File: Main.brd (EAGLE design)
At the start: 100 x 80 mm, 11 parts, among them U2 LM 1084 IT5,0, U3 LM 1084 IT3,3, X1 12V

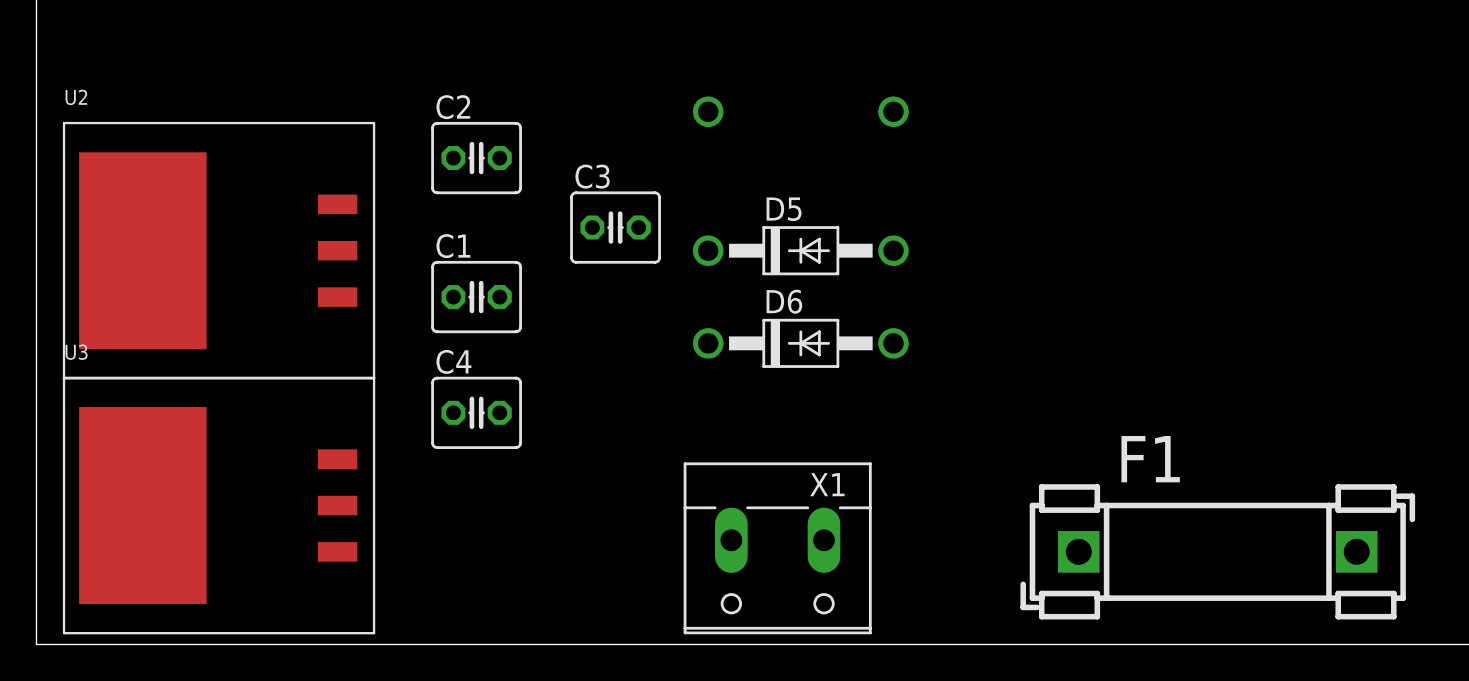
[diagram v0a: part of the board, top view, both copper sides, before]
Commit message: got rid of unneeded junctions
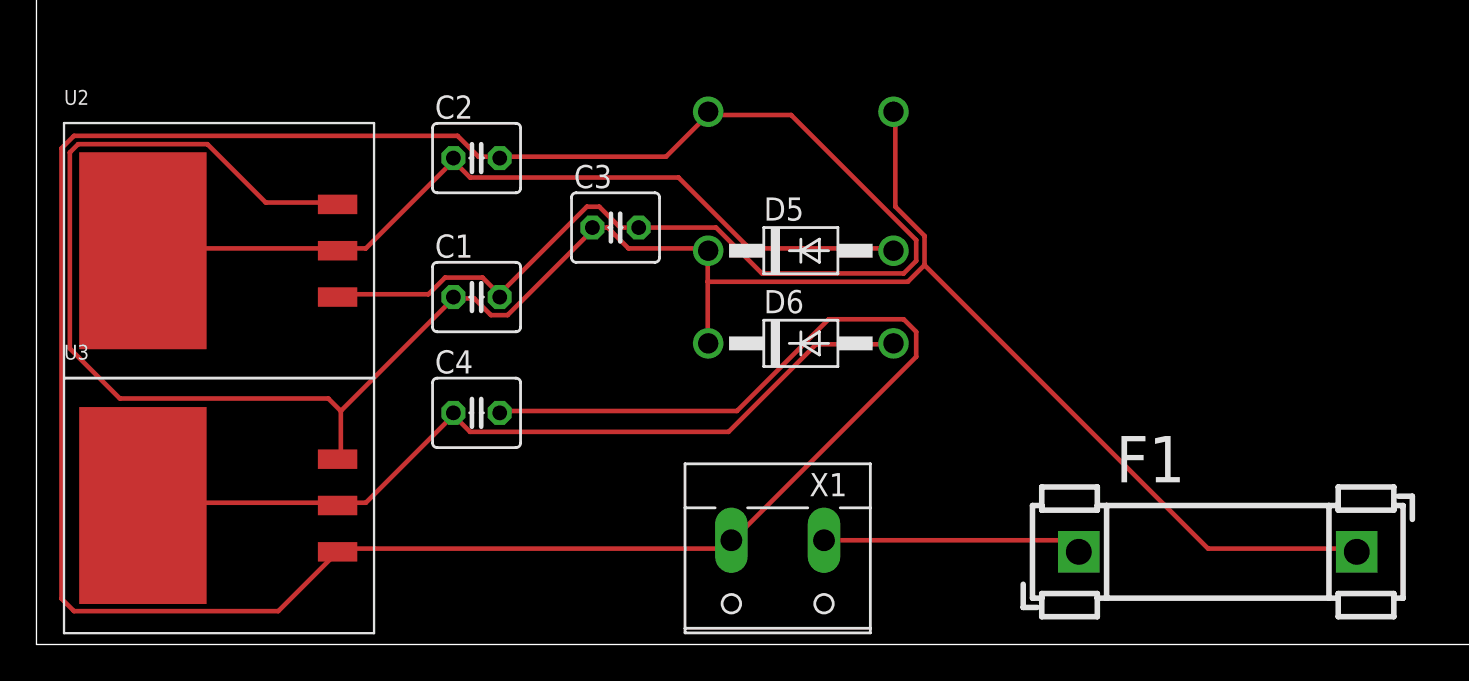
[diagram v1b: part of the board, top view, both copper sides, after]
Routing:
- net N$3: track 0.00 -> 193.5 mm
- net +12V: track 0.00 -> 128.6 mm
- net +3.3V: track 0.00 -> 45.9 mm
- net +5V: track 0.00 -> 45.5 mm
- net N$1: track 0.00 -> 14.3 mm

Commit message: fixed it... misleading warnings due to unneeded wires
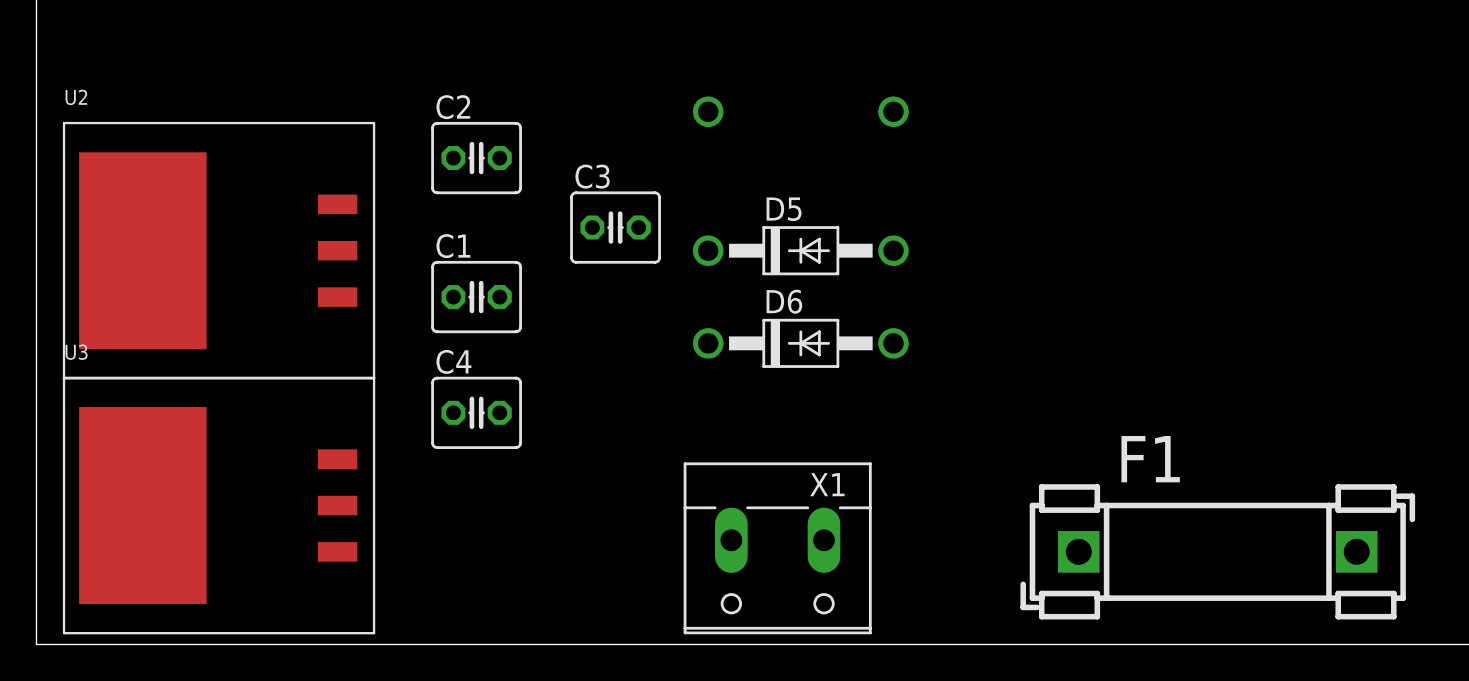
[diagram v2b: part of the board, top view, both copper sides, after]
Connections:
- net N$3 renamed GND
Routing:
- net GND: track 193.5 -> 0.00 mm
- net +12V: track 128.6 -> 0.00 mm
- net +3.3V: track 45.9 -> 0.00 mm
- net +5V: track 45.5 -> 0.00 mm
- net N$1: track 14.3 -> 0.00 mm

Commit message: got rid of hopefully redundant C
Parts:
- removed C3: 10uF Tant., rcl:C025-040X050
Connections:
- net +12V: no longer C3.1
- net GND: no longer C3.2
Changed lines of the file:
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@@
 <element name="C1" library="rcl" package="C025-040X050" value="10uF Tant." x="24.13" y="19.05"/>
 <element name="C2" library="rcl" package="C025-040X050" value="10uF Tant." x="24.13" y="26.67"/>
-<element name="C3" library="rcl" package="C025-040X050" value="10uF Tant." x="31.75" y="22.86"/>
 <element name="C4" library="rcl" package="C025-040X050" value="10uF Tant." x="24.13" y="12.7"/>
 <element name="D5" library="diode" package="DO41-10" value="1N4004" x="41.91" y="21.59"/>
@@
 <contactref element="D6" pad="C"/>
 <contactref element="U3" pad="3"/>
-<contactref element="C1" pad="1"/>
-<contactref element="C3" pad="1"/>
 <contactref element="D5" pad="C"/>
 <contactref element="D1" pad="C"/>
 <contactref element="F1" pad="2"/>
+<contactref element="C1" pad="1"/>
 <wire x1="46.99" y1="29.21" x2="72.39" y2="5.08" width="0" layer="19" extent="1-1"/>
 <wire x1="36.83" y1="21.59" x2="46.99" y2="29.21" width="0" layer="19" extent="1-1"/>
 <wire x1="36.83" y1="16.51" x2="36.83" y2="21.59" width="0" layer="19" extent="1-1"/>
-<wire x1="30.48" y1="22.86" x2="36.83" y2="21.59" width="0" layer="19" extent="1-1"/>
-<wire x1="22.86" y1="19.05" x2="30.48" y2="22.86" width="0" layer="19" extent="1-1"/>
+<wire x1="22.86" y1="19.05" x2="36.83" y2="21.59" width="0" layer="19" extent="1-1"/>
 <wire x1="16.51" y1="24.13" x2="22.86" y2="19.05" width="0" layer="19" extent="1-1"/>
 <wire x1="16.51" y1="10.16" x2="22.86" y2="19.05" width="0" layer="19" extent="1-1"/>
@@
 <signal name="GND">
 <contactref element="X1" pad="2"/>
-<contactref element="C1" pad="2"/>
 <contactref element="C4" pad="2"/>
 <contactref element="C2" pad="2"/>
-<contactref element="C3" pad="2"/>
 <contactref element="U3" pad="1"/>
 <contactref element="U2" pad="1"/>
 <contactref element="D1" pad="A"/>
-<wire x1="33.02" y1="22.86" x2="36.83" y2="29.21" width="0" layer="19" extent="1-1"/>
-<wire x1="25.4" y1="26.67" x2="33.02" y2="22.86" width="0" layer="19" extent="1-1"/>
+<contactref element="C1" pad="2"/>
+<wire x1="25.4" y1="26.67" x2="36.83" y2="29.21" width="0" layer="19" extent="1-1"/>
 <wire x1="25.4" y1="19.05" x2="25.4" y2="26.67" width="0" layer="19" extent="1-1"/>
 <wire x1="25.4" y1="12.7" x2="25.4" y2="19.05" width="0" layer="19" extent="1-1"/>

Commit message: finally got connections without wires
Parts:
- added R1: 4711, resistor:0617/22
- moved F1 90.9 mm to (-31.8, 24.1)
- moved D1 83.9 mm to (-40.6, 44.5), flipped to the top
- moved X1 83.8 mm to (-40.6, 25.4), turned to 0 degrees
- moved D6 82.4 mm to (-31.8, 53.3)
- moved C1 71.8 mm to (-45.7, 35.6)
- moved D5 68.7 mm to (-19.1, 53.3)
- moved C4 63.8 mm to (-30.5, 45.7)
- moved U3 49.5 mm to (-38.1, 7.62)
- moved C2 48.4 mm to (-20.3, 45.7)
- moved U2 34.7 mm to (-20.3, 7.62)
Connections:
- net +12V: now also R1.1
- net GND: now also R1.2
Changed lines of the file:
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@@
 <description language="de">&lt;b&gt;EAGLE Design Rules&lt;/b&gt;
 &lt;p&gt;
-Die Standard-Design-Rules sind so gewÃ¤hlt, dass sie fÃ¼r
+Die Standard-Design-Rules sind so gewählt, dass sie für
 die meisten Anwendungen passen. Sollte ihre Platine
 besondere Anforderungen haben, treffen Sie die erforderlichen
@@
 <autorouter>
 <pass name="Default">
-<param name="RoutingGrid" value="12.5mil"/>
+<param name="RoutingGrid" value="50mil"/>
 <param name="AutoGrid" value="1"/>
 <param name="Efforts" value="0"/>
 <param name="TopRouterVariant" value="1"/>
 <param name="tpViaShape" value="round"/>
-<param name="PrefDir.1" value="|"/>
+<param name="PrefDir.1" value="a"/>
 <param name="PrefDir.2" value="0"/>
 <param name="PrefDir.3" value="0"/>
@@
 <param name="PrefDir.14" value="0"/>
 <param name="PrefDir.15" value="0"/>
-<param name="PrefDir.16" value="0"/>
+<param name="PrefDir.16" value="a"/>
 <param name="cfVia" value="8"/>
 <param name="cfNonPref" value="5"/>
@@
 </autorouter>
 <elements>
-<element name="C1" library="rcl" package="C025-040X050" value="10uF Tant." x="24.13" y="19.05"/>
-<element name="C2" library="rcl" package="C025-040X050" value="10uF Tant." x="24.13" y="26.67"/>
-<element name="C4" library="rcl" package="C025-040X050" value="10uF Tant." x="24.13" y="12.7"/>
-<element name="D5" library="diode" package="DO41-10" value="1N4004" x="41.91" y="21.59"/>
-<element name="D6" library="diode" package="DO41-10" value="1N4004" x="41.91" y="16.51"/>
-<element name="U2" library="PP_PowerIC" package="TO-263-3" value="LM 1084 IT5,0" x="11.43" y="21.59"/>
-<element name="U3" library="PP_PowerIC" package="TO-263-3" value="LM 1084 IT3,3" x="11.43" y="7.62"/>
-<element name="X1" library="con-wago-508" package="W237-132" value="12V" x="40.64" y="5.08" rot="R180">
-<attribute name="OC_NEWARK" value="unknown" x="40.64" y="5.08" size="1.778" layer="27" rot="R180" display="off"/>
-<attribute name="MPN" value="" x="40.64" y="5.08" size="1.778" layer="27" rot="R180" display="off"/>
-<attribute name="MF" value="" x="40.64" y="5.08" size="1.778" layer="27" rot="R180" display="off"/>
-<attribute name="OC_FARNELL" value="unknown" x="40.64" y="5.08" size="1.778" layer="27" rot="R180" display="off"/>
+<element name="C1" library="rcl" package="C025-040X050" value="10uF Tant." x="-45.72" y="35.56"/>
+<element name="C2" library="rcl" package="C025-040X050" value="10uF Tant." x="-20.32" y="45.72"/>
+<element name="C4" library="rcl" package="C025-040X050" value="10uF Tant." x="-30.48" y="45.72"/>
+<element name="D1" library="diode" package="DO41-10" value="1N4004" x="-40.64" y="44.45"/>
+<element name="D5" library="diode" package="DO41-10" value="1N4004" x="-19.05" y="53.34"/>
+<element name="D6" library="diode" package="DO41-10" value="1N4004" x="-31.75" y="53.34"/>
+<element name="F1" library="fuse" package="FUSE_HOLDER_5X20MM" value="10A" x="-31.75" y="24.13">
+<attribute name="OC_NEWARK" value="unknown" x="-31.75" y="24.13" size="1.778" layer="27" display="off"/>
+<attribute name="MPN" value="" x="-31.75" y="24.13" size="1.778" layer="27" display="off"/>
+<attribute name="MF" value="" x="-31.75" y="24.13" size="1.778" layer="27" display="off"/>
+<attribute name="OC_FARNELL" value="unknown" x="-31.75" y="24.13" size="1.778" layer="27" display="off"/>
 </element>
-<element name="D1" library="diode" package="DO41-10" value="1N4004" x="41.91" y="29.21" rot="MR0"/>
-<element name="F1" library="fuse" package="FUSE_HOLDER_5X20MM" value="10A" x="57.15" y="5.08">
-<attribute name="OC_NEWARK" value="unknown" x="57.15" y="5.08" size="1.778" layer="27" display="off"/>
-<attribute name="MPN" value="" x="57.15" y="5.08" size="1.778" layer="27" display="off"/>
-<attribute name="MF" value="" x="57.15" y="5.08" size="1.778" layer="27" display="off"/>
-<attribute name="OC_FARNELL" value="unknown" x="57.15" y="5.08" size="1.778" layer="27" display="off"/>
+<element name="R1" library="resistor" package="0617/22" value="4711" x="-25.4" y="35.56"/>
+<element name="U2" library="PP_PowerIC" package="TO-263-3" value="LM 1084 IT5,0" x="-20.32" y="7.62"/>
+<element name="U3" library="PP_PowerIC" package="TO-263-3" value="LM 1084 IT3,3" x="-38.1" y="7.62"/>
+<element name="X1" library="con-wago-508" package="W237-132" value="12V" x="-40.64" y="25.4">
+<attribute name="OC_NEWARK" value="unknown" x="-40.64" y="25.4" size="1.778" layer="27" display="off"/>
+<attribute name="MPN" value="" x="-40.64" y="25.4" size="1.778" layer="27" display="off"/>
+<attribute name="MF" value="" x="-40.64" y="25.4" size="1.778" layer="27" display="off"/>
+<attribute name="OC_FARNELL" value="unknown" x="-40.64" y="25.4" size="1.778" layer="27" display="off"/>
 </element>
 </elements>
@@
 <contactref element="D5" pad="A"/>
 <contactref element="C2" pad="1"/>
+<contactref element="U2" pad="2"/>
 <contactref element="U2" pad="4"/>
-<contactref element="U2" pad="2"/>
-<wire x1="22.86" y1="26.67" x2="46.99" y2="21.59" width="0" layer="19" extent="1-1"/>
-<wire x1="16.51" y1="21.59" x2="22.86" y2="26.67" width="0" layer="19" extent="1-1"/>
-<wire x1="5.835" y1="21.59" x2="16.51" y2="21.59" width="0" layer="19" extent="1-1"/>
+<wire x1="-21.59" y1="45.72" x2="-13.97" y2="53.34" width="0" layer="19" extent="1-1"/>
+<wire x1="-25.915" y1="7.62" x2="-21.59" y2="45.72" width="0" layer="19" extent="1-1"/>
+<wire x1="-15.24" y1="7.62" x2="-25.915" y2="7.62" width="0" layer="19" extent="1-1"/>
 </signal>
 <signal name="+3.3V">
 <contactref element="D6" pad="A"/>
 <contactref element="C4" pad="1"/>
+<contactref element="U3" pad="2"/>
 <contactref element="U3" pad="4"/>
-<contactref element="U3" pad="2"/>
-<wire x1="22.86" y1="12.7" x2="46.99" y2="16.51" width="0" layer="19" extent="1-1"/>
-<wire x1="16.51" y1="7.62" x2="22.86" y2="12.7" width="0" layer="19" extent="1-1"/>
-<wire x1="5.835" y1="7.62" x2="16.51" y2="7.62" width="0" layer="19" extent="1-1"/>
+<wire x1="-33.02" y1="7.62" x2="-43.695" y2="7.62" width="0" layer="19" extent="1-1"/>
+<wire x1="-31.75" y1="45.72" x2="-33.02" y2="7.62" width="0" layer="19" extent="1-1"/>
+<wire x1="-26.67" y1="53.34" x2="-31.75" y2="45.72" width="0" layer="19" extent="1-1"/>
 </signal>
 <signal name="+12V">
-<contactref element="U2" pad="3"/>
 <contactref element="D6" pad="C"/>
 <contactref element="U3" pad="3"/>
 <contactref element="D5" pad="C"/>
+<contactref element="U2" pad="3"/>
 <contactref element="D1" pad="C"/>
 <contactref element="F1" pad="2"/>
 <contactref element="C1" pad="1"/>
-<wire x1="46.99" y1="29.21" x2="72.39" y2="5.08" width="0" layer="19" extent="1-1"/>
-<wire x1="36.83" y1="21.59" x2="46.99" y2="29.21" width="0" layer="19" extent="1-1"/>
-<wire x1="36.83" y1="16.51" x2="36.83" y2="21.59" width="0" layer="19" extent="1-1"/>
-<wire x1="22.86" y1="19.05" x2="36.83" y2="21.59" width="0" layer="19" extent="1-1"/>
-<wire x1="16.51" y1="24.13" x2="22.86" y2="19.05" width="0" layer="19" extent="1-1"/>
-<wire x1="16.51" y1="10.16" x2="22.86" y2="19.05" width="0" layer="19" extent="1-1"/>
+<contactref element="R1" pad="1"/>
+<wire x1="-36.83" y1="53.34" x2="-24.13" y2="53.34" width="0" layer="19" extent="1-1"/>
+<wire x1="-45.72" y1="44.45" x2="-36.83" y2="53.34" width="0" layer="19" extent="1-1"/>
+<wire x1="-46.99" y1="35.56" x2="-45.72" y2="44.45" width="0" layer="19" extent="1-1"/>
+<wire x1="-36.83" y1="35.56" x2="-46.99" y2="35.56" width="0" layer="19" extent="1-1"/>
+<wire x1="-16.51" y1="24.13" x2="-36.83" y2="35.56" width="0" layer="19" extent="1-1"/>
+<wire x1="-15.24" y1="10.16" x2="-16.51" y2="24.13" width="0" layer="19" extent="1-1"/>
+<wire x1="-33.02" y1="10.16" x2="-15.24" y2="10.16" width="0" layer="19" extent="1-1"/>
 </signal>
 <signal name="N$1">
 <contactref element="X1" pad="1"/>
 <contactref element="F1" pad="1"/>
-<wire x1="43.18" y1="5.715" x2="57.15" y2="5.08" width="0" layer="19" extent="1-1"/>
+<wire x1="-31.75" y1="24.13" x2="-43.18" y2="24.765" width="0" layer="19" extent="1-1"/>
 </signal>
 <signal name="GND">
-<contactref element="X1" pad="2"/>
-<contactref element="C4" pad="2"/>
-<contactref element="C2" pad="2"/>
 <contactref element="U3" pad="1"/>
 <contactref element="U2" pad="1"/>
+<contactref element="X1" pad="2"/>
+<contactref element="C2" pad="2"/>
+<contactref element="C4" pad="2"/>
 <contactref element="D1" pad="A"/>
 <contactref element="C1" pad="2"/>
-<wire x1="25.4" y1="26.67" x2="36.83" y2="29.21" width="0" layer="19" extent="1-1"/>
-<wire x1="25.4" y1="19.05" x2="25.4" y2="26.67" width="0" layer="19" extent="1-1"/>
-<wire x1="25.4" y1="12.7" x2="25.4" y2="19.05" width="0" layer="19" extent="1-1"/>
-<wire x1="16.51" y1="19.05" x2="25.4" y2="19.05" width="0" layer="19" extent="1-1"/>
-<wire x1="16.51" y1="5.08" x2="25.4" y2="12.7" width="0" layer="19" extent="1-1"/>
-<wire x1="38.1" y1="5.715" x2="25.4" y2="12.7" width="0" layer="19" extent="1-1"/>
+<contactref element="R1" pad="2"/>
+<wire x1="-15.24" y1="5.08" x2="-33.02" y2="5.08" width="0" layer="19" extent="1-1"/>
+<wire x1="-38.1" y1="24.765" x2="-33.02" y2="5.08" width="0" layer="19" extent="1-1"/>
+<wire x1="-44.45" y1="35.56" x2="-38.1" y2="24.765" width="0" layer="19" extent="1-1"/>
+<wire x1="-35.56" y1="44.45" x2="-44.45" y2="35.56" width="0" layer="19" extent="1-1"/>
+<wire x1="-29.21" y1="45.72" x2="-35.56" y2="44.45" width="0" layer="19" extent="1-1"/>
+<wire x1="-19.05" y1="45.72" x2="-29.21" y2="45.72" width="0" layer="19" extent="1-1"/>
+<wire x1="-13.97" y1="35.56" x2="-19.05" y2="45.72" width="0" layer="19" extent="1-1"/>
 </signal>
 </signals>
